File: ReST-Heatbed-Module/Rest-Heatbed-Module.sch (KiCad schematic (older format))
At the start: 18 parts, among them P1 02-SCREW-TERM, P2 CONN_02X03, P3 02-SCREW-TERM, P4 01X02-MALE, P5 02-SCREW-TERM, P6 CONN_02X02, Q1 Q_BSH105/IRLML2502, Q2 Q_AOT240L

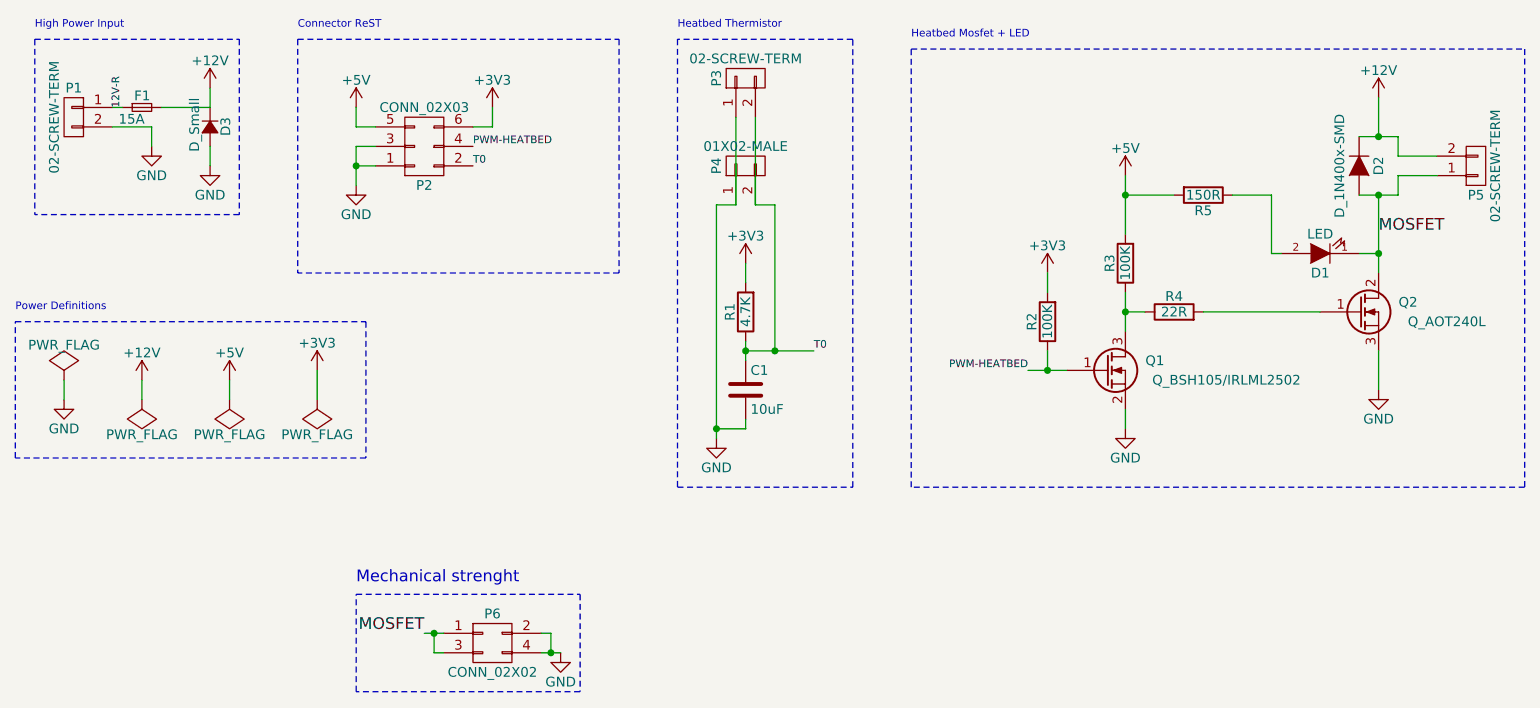
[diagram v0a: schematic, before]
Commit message: Changes in Heatbed and Heater + F1 and F4 Pinout table with functions
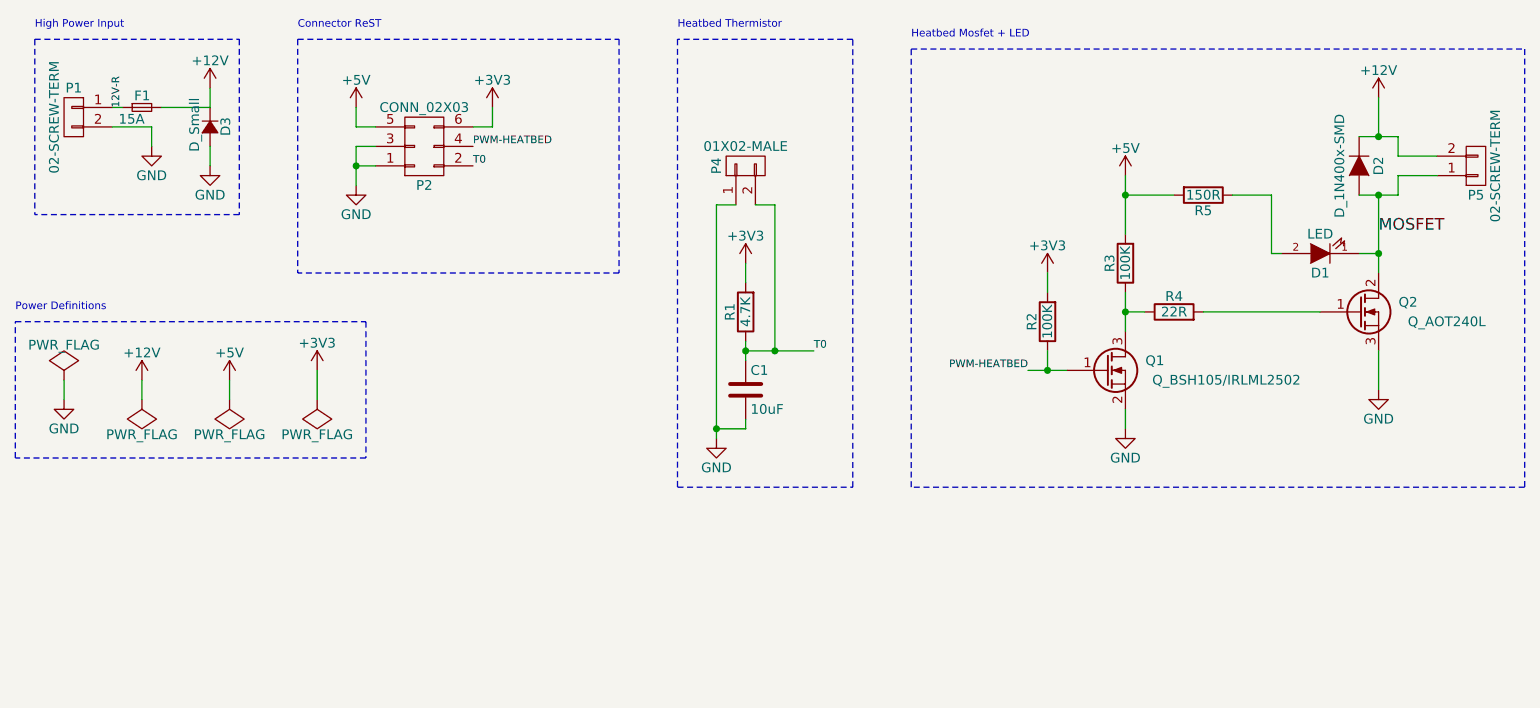
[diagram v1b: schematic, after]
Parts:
- removed P3: 02-SCREW-TERM, ReST-Library:pt_1,5-2-3,5-h, symbol CONN_01X02
- removed P6: CONN_02X02, ReST-Library:bb02-hp04, symbol CONN_02X02
- P4: footprint Pin_Headers:Pin_Header_Straight_1x02 -> ReST-Library:bb02-hy02a
- R1, R2, R3, R4, R5: footprint Resistors_SMD:R_0805_HandSoldering -> Resistors_SMD:R_0603_HandSoldering
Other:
- note removed: "Mechanical strenght"
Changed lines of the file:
@@
 F 0 "R4" V 8680 3550 50  0000 C CNN
 F 1 "22R" V 8600 3550 50  0000 C CNN
-F 2 "Resistors_SMD:R_0805_HandSoldering" V 8530 3550 50  0001 C CNN
+F 2 "Resistors_SMD:R_0603_HandSoldering" V 8530 3550 50  0001 C CNN
 F 3 "" H 8600 3550 50  0000 C CNN
 	1    8600 3550
@@
 $EndComp
 $Comp
-L CONN_01X02 P3
-U 1 1 56A6ACF0
-P 6400 2350
-F 0 "P3" H 6400 2500 50  0000 C CNN
-F 1 "02-SCREW-TERM" V 6500 2350 50  0000 C CNN
-F 2 "ReST-Library:pt_1,5-2-3,5-h" H 6400 2350 50  0001 C CNN
-F 3 "" H 6400 2350 50  0000 C CNN
-	1    6400 2350
-	0    -1   -1   0
-$EndComp
-$Comp
 L CONN_01X02 P4
 U 1 1 56A6AD1A
@@
 F 0 "P4" H 6400 2950 50  0000 C CNN
 F 1 "01X02-MALE" V 6500 2800 50  0000 C CNN
-F 2 "Pin_Headers:Pin_Header_Straight_1x02" H 6400 2800 50  0001 C CNN
+F 2 "ReST-Library:bb02-hy02a" H 6400 2800 50  0001 C CNN
 F 3 "" H 6400 2800 50  0000 C CNN
 	1    6400 2800
@@
 F 0 "R1" V 6480 3550 50  0000 C CNN
 F 1 "4.7K" V 6400 3550 50  0000 C CNN
-F 2 "Resistors_SMD:R_0805_HandSoldering" V 6330 3550 50  0001 C CNN
+F 2 "Resistors_SMD:R_0603_HandSoldering" V 6330 3550 50  0001 C CNN
 F 3 "" H 6400 3550 50  0000 C CNN
 	1    6400 3550
@@
 F 0 "R2" V 8030 3600 50  0000 C CNN
 F 1 "100K" V 7950 3600 50  0000 C CNN
-F 2 "Resistors_SMD:R_0805_HandSoldering" V 7880 3600 50  0001 C CNN
+F 2 "Resistors_SMD:R_0603_HandSoldering" V 7880 3600 50  0001 C CNN
 F 3 "" H 7950 3600 50  0000 C CNN
 	1    7950 3600
@@
 F 0 "R3" V 8430 3300 50  0000 C CNN
 F 1 "100K" V 8350 3300 50  0000 C CNN
-F 2 "Resistors_SMD:R_0805_HandSoldering" V 8280 3300 50  0001 C CNN
+F 2 "Resistors_SMD:R_0603_HandSoldering" V 8280 3300 50  0001 C CNN
 F 3 "" H 8350 3300 50  0000 C CNN
 	1    8350 3300
@@
 F 0 "R5" V 8830 2950 50  0000 C CNN
 F 1 "150R" V 8750 2950 50  0000 C CNN
-F 2 "Resistors_SMD:R_0805_HandSoldering" V 8680 2950 50  0001 C CNN
+F 2 "Resistors_SMD:R_0603_HandSoldering" V 8680 2950 50  0001 C CNN
 F 3 "" H 8750 2950 50  0000 C CNN
 	1    8750 2950
@@
 	3350 2600 3350 2700
 Wire Wire Line
-	6350 3000 6350 2550
-Wire Wire Line
-	6450 2550 6450 3000
-Wire Wire Line
 	6400 3400 6400 3300
 Wire Wire Line
@@
 	9950 2750 9750 2750
 Wire Wire Line
-	9750 2750 9750 2650
-Wire Wire Line
-	9750 2650 9550 2650
+	9750 2650 9750 2750
+Wire Wire Line
+	9550 2650 9750 2650
 Wire Wire Line
 	9950 2850 9750 2850
 Wire Wire Line
-	9750 2850 9750 2950
-Wire Wire Line
-	9750 2950 9550 2950
+	9750 2950 9750 2850
+Wire Wire Line
+	9550 2950 9750 2950
 Wire Wire Line
 	9650 2450 9650 2650
@@
 Wire Wire Line
 	5100 2600 5100 2500
-$Comp
-L CONN_02X02 P6
-U 1 1 5739BD0D
-P 5100 5250
-F 0 "P6" H 5100 5400 50  0000 C CNN
-F 1 "CONN_02X02" H 5100 5100 50  0000 C CNN
-F 2 "ReST-Library:bb02-hp04" H 5100 4050 50  0001 C CNN
-F 3 "" H 5100 4050 50  0000 C CNN
-	1    5100 5250
-	1    0    0    -1
-$EndComp
 Text Label 9650 3150 0    60   ~ 0
 MOSFET
-Text Label 4750 5200 2    60   ~ 0
-MOSFET
-Wire Wire Line
-	4750 5200 4850 5200
-Wire Wire Line
-	4850 5300 4800 5300
-Wire Wire Line
-	4800 5300 4800 5200
-Connection ~ 4800 5200
-$Comp
-L GND #PWR022
-U 1 1 5739C9F0
-P 5450 5300
-F 0 "#PWR022" H 5450 5050 50  0001 C CNN
-F 1 "GND" H 5450 5150 50  0000 C CNN
-F 2 "" H 5450 5300 50  0000 C CNN
-F 3 "" H 5450 5300 50  0000 C CNN
-	1    5450 5300
-	1    0    0    -1
-$EndComp
-Wire Wire Line
-	5350 5300 5450 5300
-Wire Wire Line
-	5400 5300 5400 5200
-Wire Wire Line
-	5400 5200 5350 5200
-Connection ~ 5400 5300
-Wire Notes Line
-	4400 5000 5550 5000
-Wire Notes Line
-	5550 5000 5550 5500
-Wire Notes Line
-	5550 5500 4400 5500
-Wire Notes Line
-	4400 5500 4400 5000
-Text Notes 4400 4950 0    60   ~ 0
-Mechanical strenght
 Text Label 3200 2500 1    39   ~ 0
 12V-R
